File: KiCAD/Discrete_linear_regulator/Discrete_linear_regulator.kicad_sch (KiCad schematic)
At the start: 18 parts, among them J1 Conn_01x06, Q1 PZT2222AT3G, Q2 BC857, Q3 BC857, Q4 PZT2222AT3G, Q5 PZT2907AT3G, Q6 BC847, Q7 BC847, Q8 PZT2907AT3G, U1 LM4562

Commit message: Worked a bit on the main board
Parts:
- C1, C3: footprint (none) -> Capacitor_SMD:C_0402_1005Metric
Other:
- note added: "For +5V: Rxx = Rxx = xxΩ Rxx = Rxx = xxΩ"
- note added: "Or +5V"
- note added: "Or +8V"
- note added: "Or -5V"
- note added: "Or -8V"
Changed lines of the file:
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@@
+    (effects (font (size 1.27 1.27)) (justify left bottom))
+  )
+  (text "Or +5V" (at 163.83 50.8 0)
     (effects (font (size 1.27 1.27)) (justify left bottom))
   )
@@
     (effects (font (size 1.27 1.27)) (justify left bottom))
   )
+  (text "Or -5V" (at 195.58 160.02 0)
+    (effects (font (size 1.27 1.27)) (justify left bottom))
+  )
+  (text "For +5V:\nRxx = Rxx = xxΩ\nRxx = Rxx = xxΩ" (at 185.42 49.53 0)
+    (effects (font (size 1.27 1.27)) (justify left bottom))
+  )
+  (text "Or -8V" (at 44.45 161.29 0)
+    (effects (font (size 1.27 1.27)) (justify left bottom))
+  )
   (text "10uF instead of 100uF?" (at 17.78 22.86 0)
+    (effects (font (size 1.27 1.27)) (justify left bottom))
+  )
+  (text "Or +8V" (at 36.83 52.07 0)
     (effects (font (size 1.27 1.27)) (justify left bottom))
   )
@@
     (pin "6")
     (instances
-      (project "12V_linear_regulator"
+      (project "Discrete_linear_regulator"
         (path "/19504711-657f-4df2-b2e9-322b7e64e4f7"
           (reference "J1") (unit 1)
@@
     (pin "8")
     (instances
-      (project "12V_linear_regulator"
+      (project "Discrete_linear_regulator"
         (path "/19504711-657f-4df2-b2e9-322b7e64e4f7"
           (reference "U1") (unit 1)
@@
       (effects (font (size 1.27 1.27)) (justify left))
     )
-    (property "Footprint" "" (at 263.8552 78.74 0)
+    (property "Footprint" "Capacitor_SMD:C_0402_1005Metric" (at 263.8552 78.74 0)
       (effects (font (size 1.27 1.27)) hide)
     )
@@
     (pin "2")
     (instances
-      (project "12V_linear_regulator"
+      (project "Discrete_linear_regulator"
         (path "/19504711-657f-4df2-b2e9-322b7e64e4f7"
           (reference "C3") (unit 1)
@@
     (pin "3")
     (instances
-      (project "12V_linear_regulator"
+      (project "Discrete_linear_regulator"
         (path "/19504711-657f-4df2-b2e9-322b7e64e4f7"
           (reference "Q7") (unit 1)
@@
       (effects (font (size 1.27 1.27)) (justify left))
     )
-    (property "Footprint" "" (at 263.8552 71.12 0)
+    (property "Footprint" "Capacitor_SMD:C_0402_1005Metric" (at 263.8552 71.12 0)
       (effects (font (size 1.27 1.27)) hide)
     )
@@
     (pin "2")
     (instances
-      (project "12V_linear_regulator"
+      (project "Discrete_linear_regulator"
         (path "/19504711-657f-4df2-b2e9-322b7e64e4f7"
           (reference "C1") (unit 1)
@@
     (pin "4")
     (instances
-      (project "12V_linear_regulator"
+      (project "Discrete_linear_regulator"
         (path "/19504711-657f-4df2-b2e9-322b7e64e4f7"
           (reference "Q1") (unit 1)
@@
     (pin "1")
     (instances
-      (project "12V_linear_regulator"
+      (project "Discrete_linear_regulator"
         (path "/19504711-657f-4df2-b2e9-322b7e64e4f7"
           (reference "#PWR09") (unit 1)
@@
     (pin "3")
     (instances
-      (project "12V_linear_regulator"
+      (project "Discrete_linear_regulator"
         (path "/19504711-657f-4df2-b2e9-322b7e64e4f7"
           (reference "Q6") (unit 1)
@@
     (pin "8")
     (instances
-      (project "12V_linear_regulator"
+      (project "Discrete_linear_regulator"
         (path "/19504711-657f-4df2-b2e9-322b7e64e4f7"
           (reference "U1") (unit 3)
@@
     (pin "3")
     (instances
-      (project "12V_linear_regulator"
+      (project "Discrete_linear_regulator"
         (path "/19504711-657f-4df2-b2e9-322b7e64e4f7"
           (reference "Q3") (unit 1)
@@
     (pin "1")
     (instances
-      (project "12V_linear_regulator"
+      (project "Discrete_linear_regulator"
         (path "/19504711-657f-4df2-b2e9-322b7e64e4f7"
           (reference "#PWR02") (unit 1)
@@
     (pin "1")
     (instances
-      (project "12V_linear_regulator"
+      (project "Discrete_linear_regulator"
         (path "/19504711-657f-4df2-b2e9-322b7e64e4f7"
           (reference "#PWR06") (unit 1)
@@
     (pin "4")
     (instances
-      (project "12V_linear_regulator"
+      (project "Discrete_linear_regulator"
         (path "/19504711-657f-4df2-b2e9-322b7e64e4f7"
           (reference "Q4") (unit 1)
@@
     (pin "1")
     (instances
-      (project "12V_linear_regulator"
+      (project "Discrete_linear_regulator"
         (path "/19504711-657f-4df2-b2e9-322b7e64e4f7"
           (reference "#PWR011") (unit 1)
@@
     (pin "2")
     (instances
-      (project "12V_linear_regulator"
+      (project "Discrete_linear_regulator"
         (path "/19504711-657f-4df2-b2e9-322b7e64e4f7"
           (reference "C2") (unit 1)
@@
     (pin "2")
     (instances
-      (project "12V_linear_regulator"
+      (project "Discrete_linear_regulator"
         (path "/19504711-657f-4df2-b2e9-322b7e64e4f7"
           (reference "C4") (unit 1)
@@
     (pin "1")
     (instances
-      (project "12V_linear_regulator"
+      (project "Discrete_linear_regulator"
         (path "/19504711-657f-4df2-b2e9-322b7e64e4f7"
           (reference "#PWR08") (unit 1)
@@
     (pin "1")
     (instances
-      (project "12V_linear_regulator"
+      (project "Discrete_linear_regulator"
         (path "/19504711-657f-4df2-b2e9-322b7e64e4f7"
           (reference "#PWR07") (unit 1)
@@
     (pin "1")
     (instances
-      (project "12V_linear_regulator"
+      (project "Discrete_linear_regulator"
         (path "/19504711-657f-4df2-b2e9-322b7e64e4f7"
           (reference "#PWR012") (unit 1)
@@
     (pin "1")
     (instances
-      (project "12V_linear_regulator"
+      (project "Discrete_linear_regulator"
         (path "/19504711-657f-4df2-b2e9-322b7e64e4f7"
           (reference "#PWR01") (unit 1)
@@
     (pin "2")
     (instances
-      (project "12V_linear_regulator"
+      (project "Discrete_linear_regulator"
         (path "/19504711-657f-4df2-b2e9-322b7e64e4f7"
           (reference "D1") (unit 1)
@@
     (pin "4")
     (instances
-      (project "12V_linear_regulator"
+      (project "Discrete_linear_regulator"
         (path "/19504711-657f-4df2-b2e9-322b7e64e4f7"
           (reference "Q5") (unit 1)
@@
     (pin "2")
     (instances
-      (project "12V_linear_regulator"
+      (project "Discrete_linear_regulator"
         (path "/19504711-657f-4df2-b2e9-322b7e64e4f7"
           (reference "R2") (unit 1)
@@
     (pin "1")
     (instances
-      (project "12V_linear_regulator"
+      (project "Discrete_linear_regulator"
         (path "/19504711-657f-4df2-b2e9-322b7e64e4f7"
           (reference "#PWR010") (unit 1)
@@
     (pin "8")
     (instances
-      (project "12V_linear_regulator"
+      (project "Discrete_linear_regulator"
         (path "/19504711-657f-4df2-b2e9-322b7e64e4f7"
           (reference "U1") (unit 2)
@@
     (pin "2")
     (instances
-      (project "12V_linear_regulator"
+      (project "Discrete_linear_regulator"
         (path "/19504711-657f-4df2-b2e9-322b7e64e4f7"
           (reference "D2") (unit 1)
@@
     (pin "1")
     (instances
-      (project "12V_linear_regulator"
+      (project "Discrete_linear_regulator"
         (path "/19504711-657f-4df2-b2e9-322b7e64e4f7"
           (reference "#PWR03") (unit 1)
@@
     (pin "4")
     (instances
-      (project "12V_linear_regulator"
+      (project "Discrete_linear_regulator"
         (path "/19504711-657f-4df2-b2e9-322b7e64e4f7"
           (reference "Q8") (unit 1)
@@
     (pin "3")
     (instances
-      (project "12V_linear_regulator"
+      (project "Discrete_linear_regulator"
         (path "/19504711-657f-4df2-b2e9-322b7e64e4f7"
           (reference "Q2") (unit 1)
@@
     (pin "1")
     (instances
-      (project "12V_linear_regulator"
+      (project "Discrete_linear_regulator"
         (path "/19504711-657f-4df2-b2e9-322b7e64e4f7"
           (reference "#PWR04") (unit 1)
@@
     (pin "2")
     (instances
-      (project "12V_linear_regulator"
+      (project "Discrete_linear_regulator"
         (path "/19504711-657f-4df2-b2e9-322b7e64e4f7"
           (reference "R1") (unit 1)
@@
     (pin "1")
     (instances
-      (project "12V_linear_regulator"
+      (project "Discrete_linear_regulator"
         (path "/19504711-657f-4df2-b2e9-322b7e64e4f7"
           (reference "#PWR05") (unit 1)

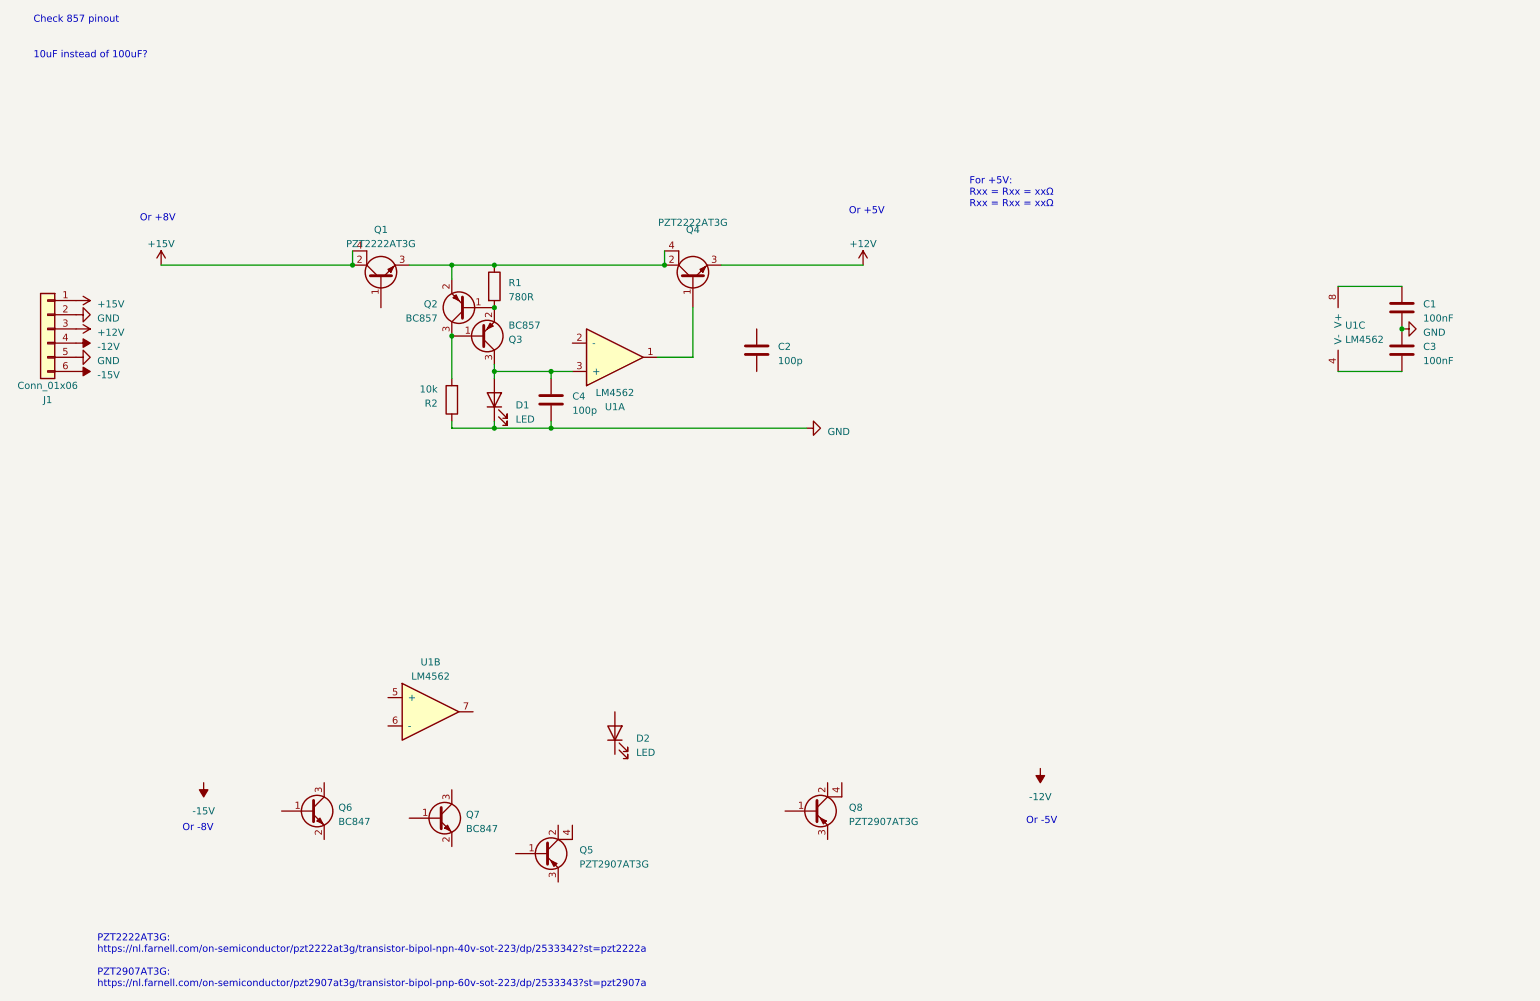
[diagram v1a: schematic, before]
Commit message: Worked on the linear voltage regulators
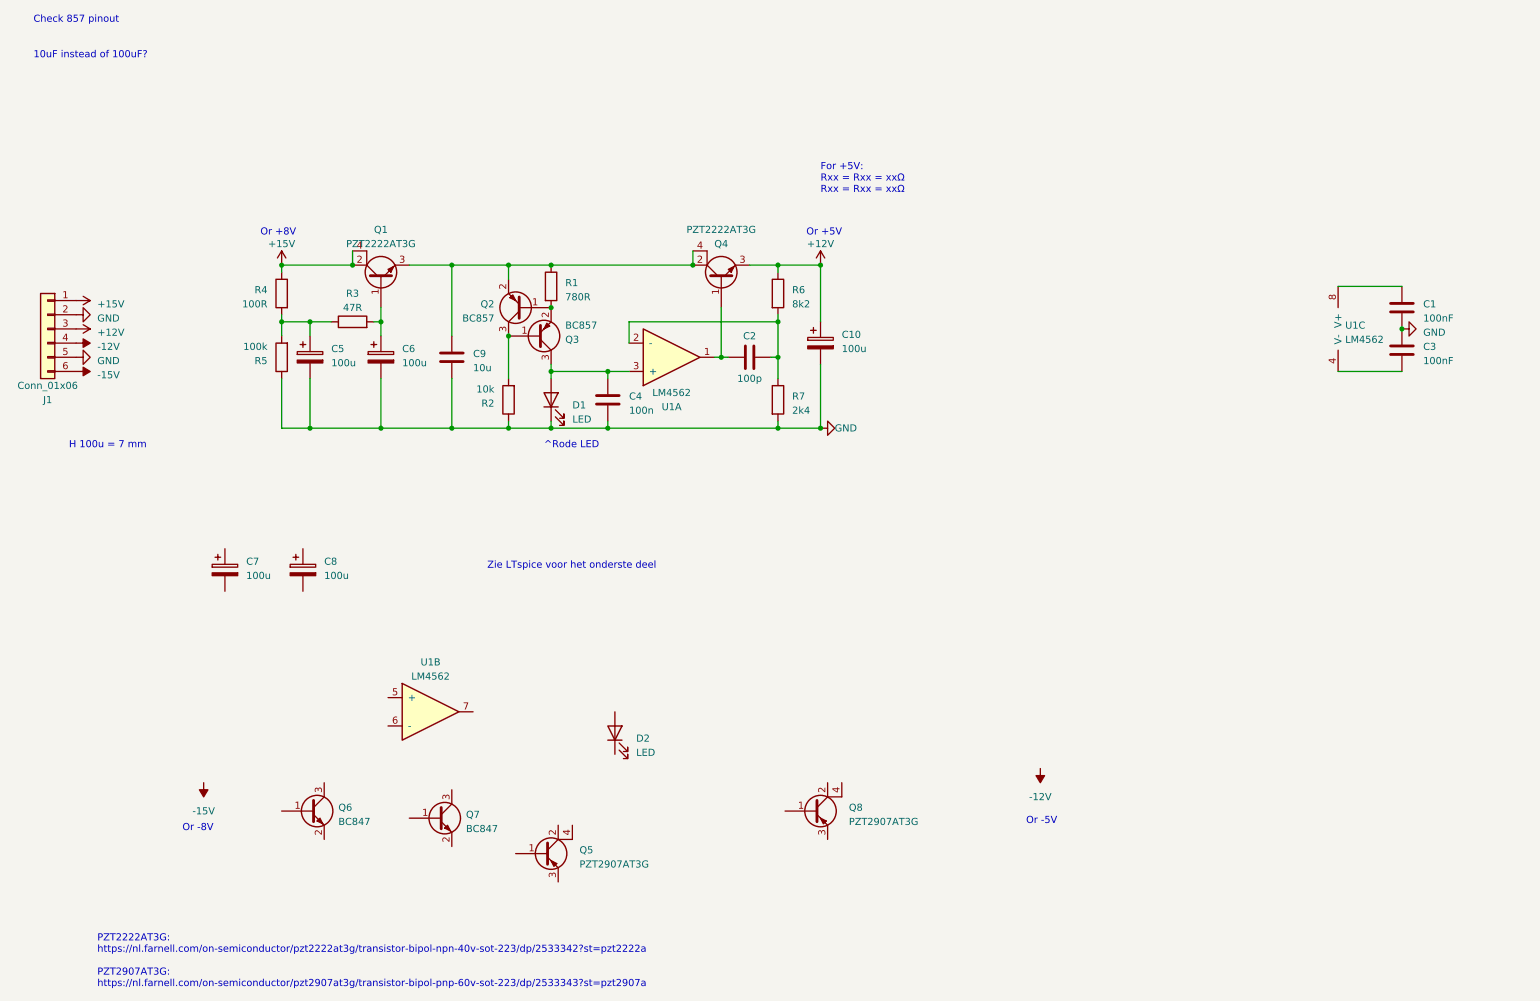
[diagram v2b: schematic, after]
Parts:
- added C10, C5, C6, C7, C8: 100u, Capacitor_THT:CP_Radial_D8.0mm_P3.50mm, symbol Device:C_Polarized
- added C9: 10u, Capacitor_SMD:C_1210_3225Metric, symbol Device:C
- added R3: 47R, Resistor_SMD:R_0402_1005Metric, symbol Device:R
- added R4: 100R, Resistor_SMD:R_0402_1005Metric, symbol Device:R
- added R5: 100k, Resistor_SMD:R_0402_1005Metric, symbol Device:R
- added R6: 8k2, Resistor_SMD:R_0402_1005Metric, symbol Device:R
- added R7: 2k4, Resistor_SMD:R_0402_1005Metric, symbol Device:R
- C4: value 100p -> 100n
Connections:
- net +12V: now also C10.1, R6.1
- net +15V: now also R4.1
- net GND: now also C10.2, C5.2, C6.2, C9.2, R5.1, R7.2
- net at Q4.1, U1.1: now also C2.2
- net at U1.2 (-): now also C2.1, R6.2, R7.1
- net at Q1.1: now also C6.1, R3.2
- net at Q1.3, Q2.2 (E), Q4.2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: now also C9.1
- new net: C5.1, R3.1, R4.2, R5.2
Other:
- note added: "H 100u = 7 mm"
- note added: "Zie LTspice voor het onderste deel"
- note added: "^Rode LED"
- moved on the sheet: C2, C4, D1, Q2, Q3, Q4, R1, R2, U1A

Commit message: sepic step file
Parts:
- removed C7, C8: 100u, Capacitor_THT:CP_Radial_D8.0mm_P3.50mm, symbol Device:C_Polarized
- removed D2: LED, symbol Device:LED
- removed Q6, Q7: BC847, Package_TO_SOT_SMD:SOT-23, symbol Transistor_BJT:BC847
- added C11, C12, C16: 100u, Capacitor_THT:CP_Radial_D8.0mm_P3.50mm, symbol Device:C_Polarized
- added C13: 10u, Capacitor_SMD:C_1210_3225Metric, symbol Device:C
- added C14: 100n, Capacitor_SMD:C_0402_1005Metric, symbol Device:C
- added C15: 100p, Capacitor_SMD:C_0402_1005Metric, symbol Device:C
- added D3: LED, symbol Device:LED
- added Q10, Q11: BC857, Package_TO_SOT_SMD:SOT-23, symbol Transistor_BJT:BC857
- added R10: 47R, Resistor_SMD:R_0402_1005Metric, symbol Device:R
- added R11: 10k, Resistor_SMD:R_0402_1005Metric, symbol Device:R
- added R12: 780R, Resistor_SMD:R_0402_1005Metric, symbol Device:R
- added R13: 8k2, Resistor_SMD:R_0402_1005Metric, symbol Device:R
- added R14: 2k4, Resistor_SMD:R_0402_1005Metric, symbol Device:R
- added R8: 100R, Resistor_SMD:R_0402_1005Metric, symbol Device:R
- added R9: 100k, Resistor_SMD:R_0402_1005Metric, symbol Device:R
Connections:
- net -12V: now also Q5.3, C16.2, R13.1
- net -15V: now also Q8.2, Q8.4, R8.1
- net GND: now also C11.1, C12.1, C13.2, C14.2, C16.1, D3.2 (A), R11.1, R14.2, R9.1
- net at Q5.1: now also U1.7, C15.2
- net at Q5.2: now also Q5.4, Q8.3, C13.1, Q10.2 (E), R12.1
- net at U1.5 (+): now also C14.1, D3.1 (K), Q11.3 (C)
- net at U1.6 (-): now also C15.1, R13.2, R14.1
- net at Q8.1: now also C12.2, R10.2
- new net: Q10.1 (B), Q11.2 (E), R12.2
- new net: Q10.3 (C), Q11.1 (B), R11.2
- new net: C11.2, R10.1, R8.2, R9.2
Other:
- note added: "For -5V: Rxx = Rxx = xxΩ Rxx = Rxx = xxΩ"
- note added: "Red LED"
- note added: "input buffer C for LM4562?"
- note removed: "Zie LTspice voor het onderste deel"
- note removed: "^Rode LED"
- moved on the sheet: Q5, Q8

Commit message: update SDD front/back end
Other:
- note added: "input decoupling capacitor for LM4562"
- note removed: "input buffer C for LM4562?"
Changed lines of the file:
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@@
     (effects (font (size 1.27 1.27)) (justify left bottom))
   )
-  (text "input buffer C for LM4562?\n" (at 246.38 59.69 0)
+  (text "input decoupling capacitor for LM4562\n" (at 240.03 60.96 0)
     (effects (font (size 1.27 1.27)) (justify left bottom))
   )
